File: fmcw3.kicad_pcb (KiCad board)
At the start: 6 copper layers, 104 x 47.7 mm, 397 parts, among them CON1 SD_Card_DM3BT, CON2 BARREL_JACK, J1 USB_C_Receptacle_USB2.0, J2 Connector_02x08, P1 SMA, P2 SMA, P5 CONN_01X01, P7 CONN_01X01, P8 CONN_01X01, SW1 B3U-1000P, SW2 B3U-1000P, U1 ADF4158, U10 HMC431LP4, U11 SKY65404, U12 PAT1220-3dB, U13 TRF37A73, U14 TQP5525, U15 SMA, U16 SKY65404, U17 LMR51420, U18 LMR51420, U19 LMR51420, U2 SolderPad_1_Circle, U20 LP5907-3.0, U21 LP2985A-10DBVR, U22 LD3920, U23 LD3920, U24 LD3920, U25 LD3920_33, U26 5400BL15B0050001E, U27 5400BL15B0050001E, U28 5400BL15B0050001E, U29 ADL5802, U3 PAT1220-6dB, U30 XC7A35T-1FTG256C, U31 SolderPad_1_Circle, U32 93LC46B, U33 FT2232H, U34 SolderPad_1_Circle, U35 SolderPad_1_Circle, U36 SolderPad_1_Circle, U38 SolderPad_1_Circle, U39 LP5907-3.0, U4 SolderPad_1_Circle, U40 W25Q128JV, U41 SolderPad_1_Circle, U42 SolderPad_1_Circle, U43 SolderPad_1_Circle, U44 SolderPad_1_Circle, U45 LT6232, U46 SolderPad_1_Circle, U47 SolderPad_1_Circle, U48 SolderPad_1_Circle, U49 SolderPad_1_Circle, U5 SolderPad_1_Circle, U6 PL133-37, U7 TLV172DCK, U8 LTC2292, U9 TRF37A73, Y1 ABM10-167-12.000MHZ-T3, Y2 ECS-TXO-32CSMV

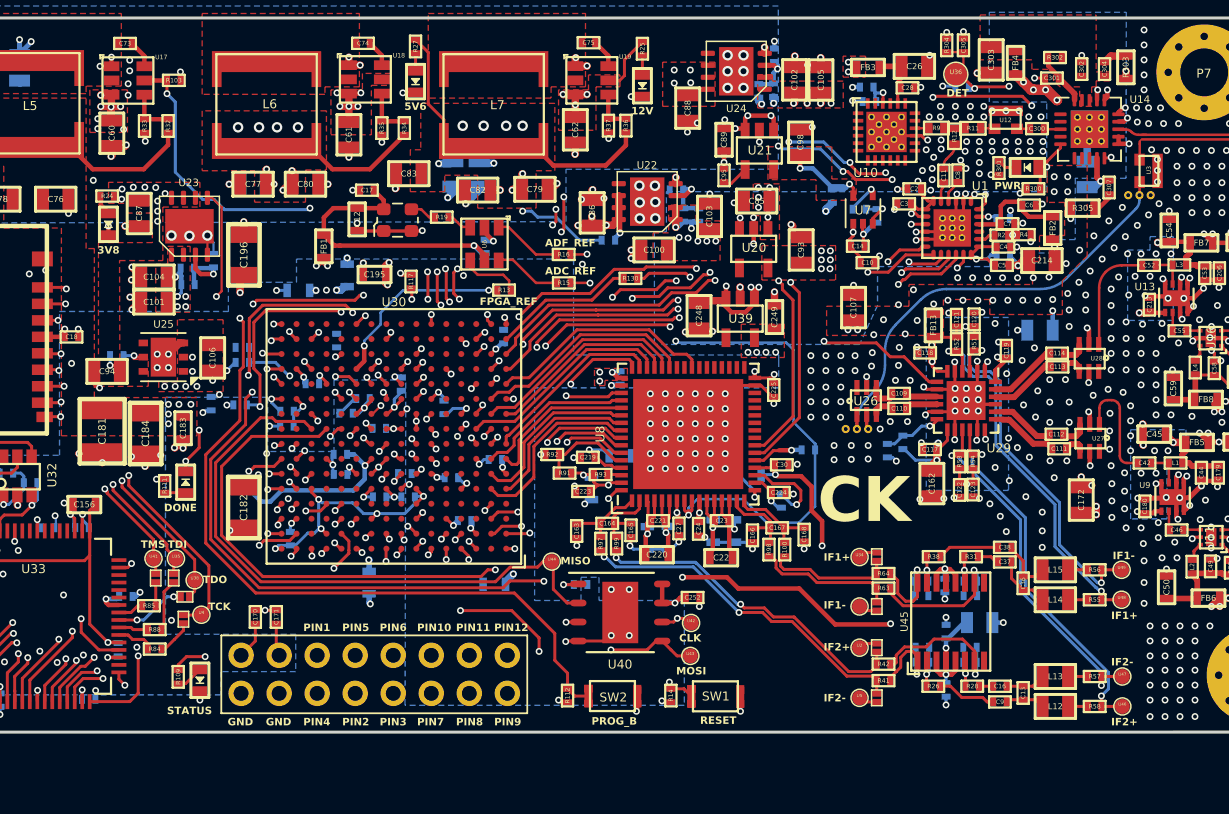
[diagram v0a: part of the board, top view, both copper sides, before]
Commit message: lt6232 is done with vias and copper pours are checked
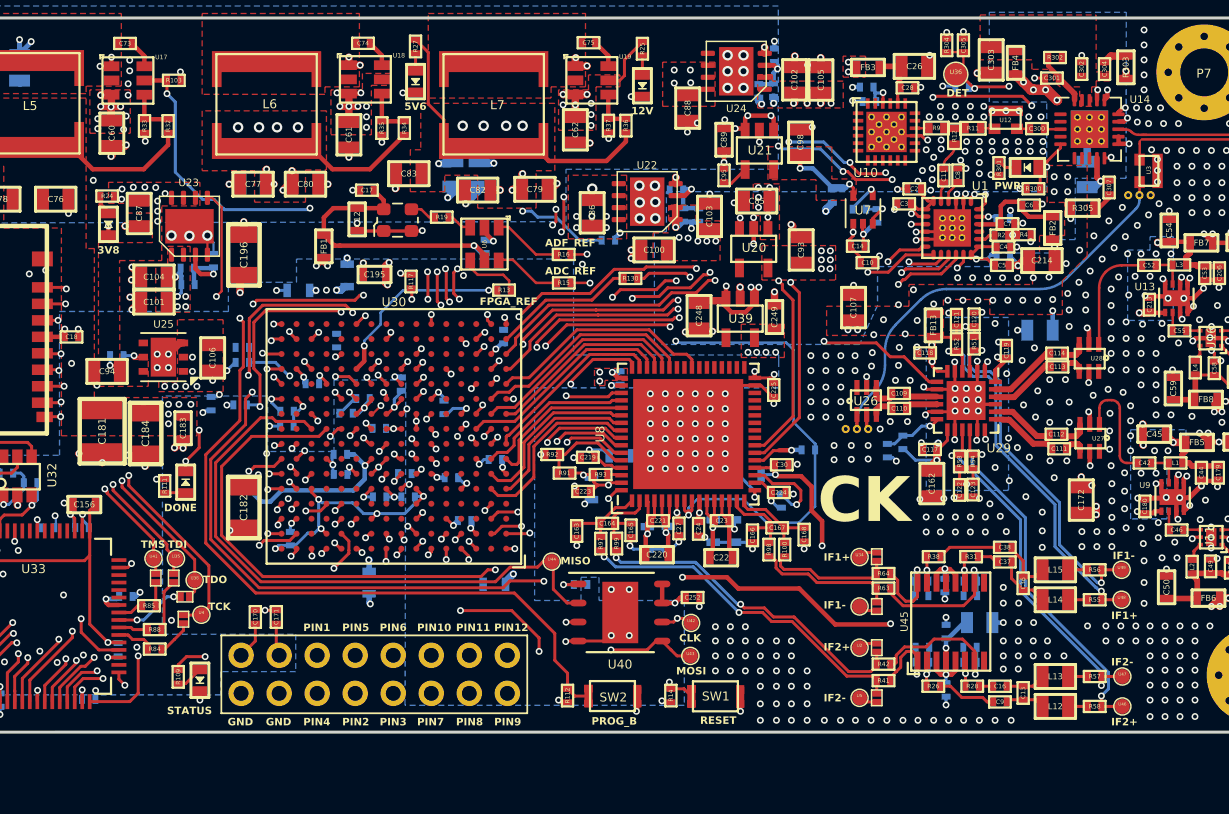
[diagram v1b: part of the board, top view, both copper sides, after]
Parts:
- Y2: value ECS-TXO-32CSMV -> ECS ECS-TXO-32CSMV-400
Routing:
- net /power/5V6: track 28.7 -> 22.3 mm, vias 13 -> 15
- net GND: track 410.7 -> 406.3 mm, vias 845 -> 928
- net /power/12V: vias 20 -> 28
